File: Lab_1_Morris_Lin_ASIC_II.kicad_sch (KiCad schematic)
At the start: 23 parts, among them J1 Q1_Header, J6 Q1_Header

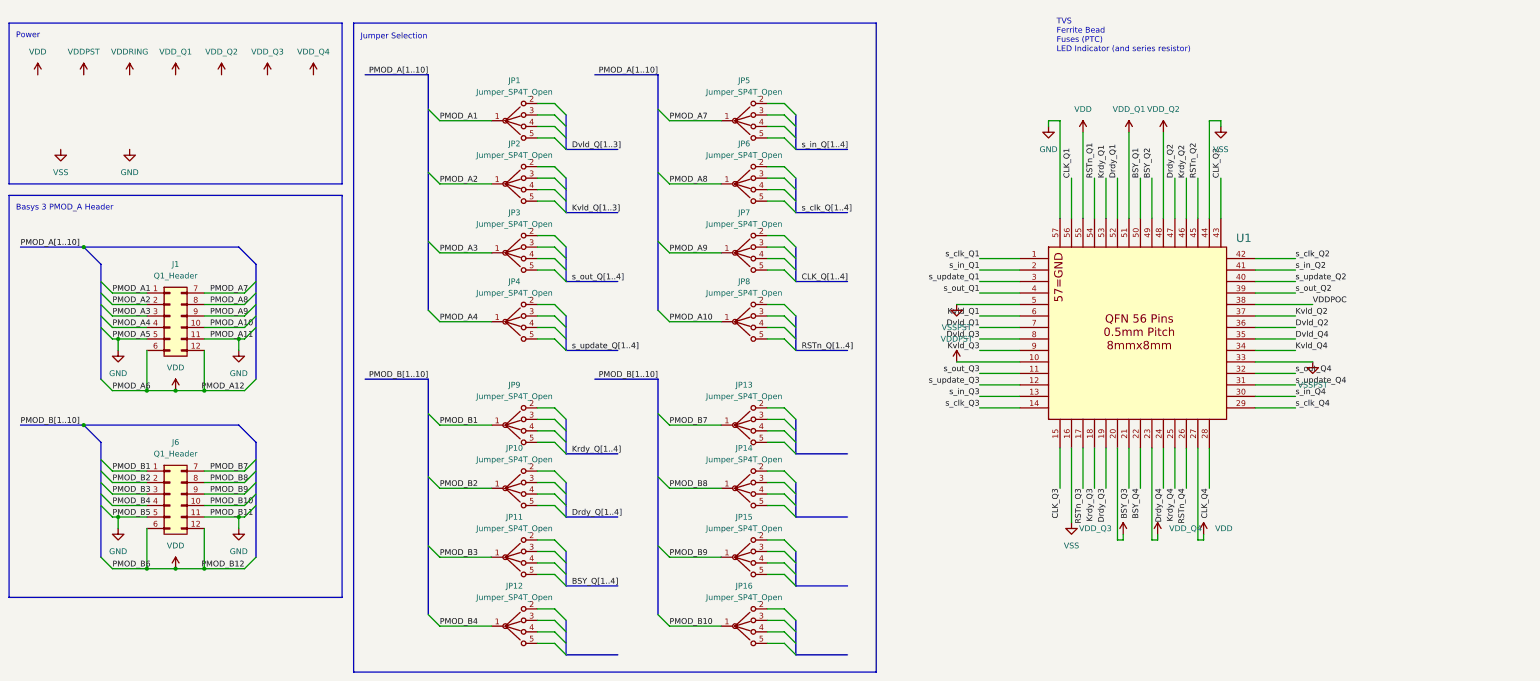
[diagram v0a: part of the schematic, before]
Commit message: Swapped to 1-of-4 Demux IC setup
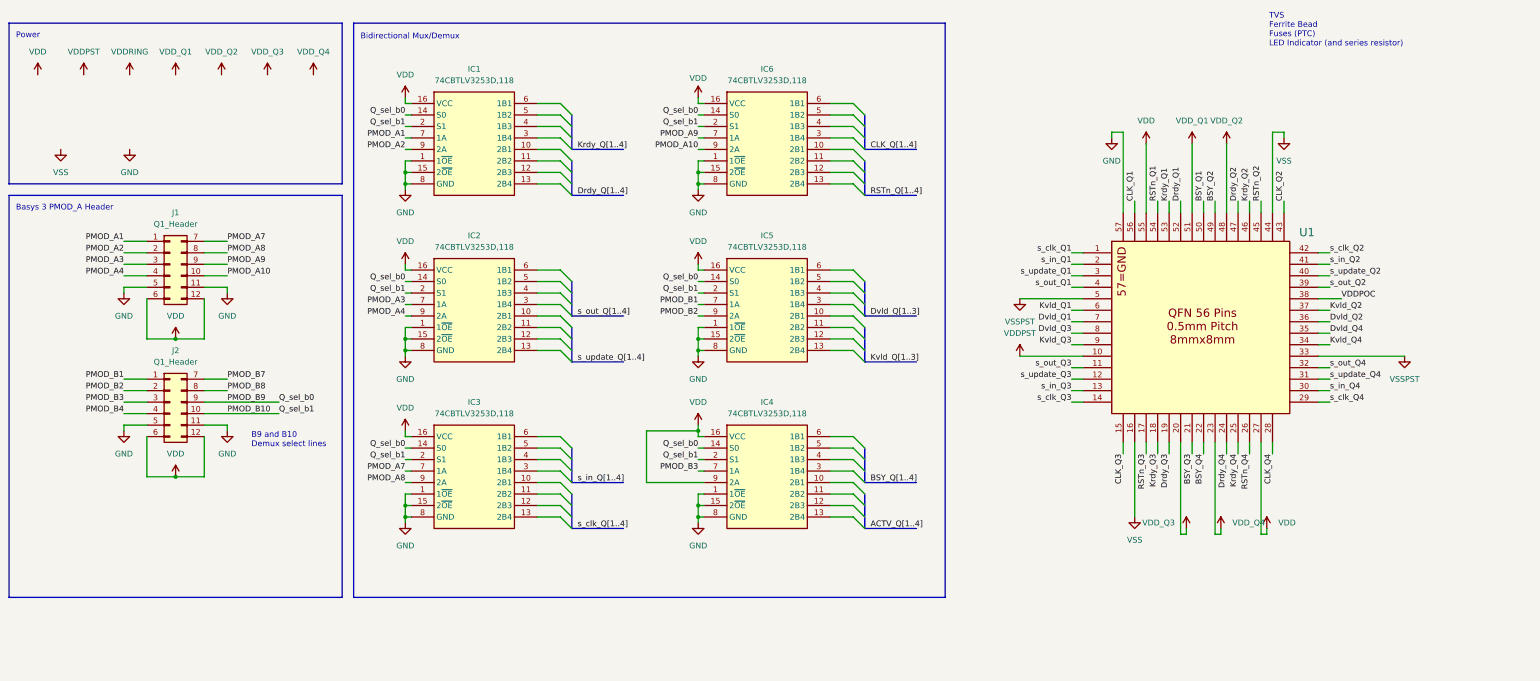
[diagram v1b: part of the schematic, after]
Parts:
- removed J6: Q1_Header, ASIC_II:PinHeader_2x06_P2.54mm_Horizontal, symbol Connector_Generic:Conn_02x06_Top_Bottom
- removed JP1, JP10, JP11, JP12, JP13, JP14, JP15, JP16, JP2, JP3, JP4, JP5, JP6, JP7, JP8, JP9: Jumper_SP4T_Open, ASIC_II:PinHeader_SP4T_1x03_P2.54mm_Vertical, symbol ASIC_II:Jumper_SP4T_Open
- added IC1, IC2, IC3, IC4, IC5, IC6: 74CBTLV3253D,118, SOIC127P600X175-16N, symbol ASIC_II:74CBTLV3253D,118
- added J2: Q1_Header, ASIC_II:PinHeader_2x06_P2.54mm_Horizontal, symbol Connector_Generic:Conn_02x06_Top_Bottom
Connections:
- net GND: now also IC1.1 (1~{OE}), IC1.15 (2~{OE}), IC1.8 (GND), IC2.1 (1~{OE}), IC2.15 (2~{OE}), IC2.8 (GND), IC3.1 (1~{OE}), IC3.15 (2~{OE}), IC3.8 (GND), IC4.1 (1~{OE}), IC4.15 (2~{OE}), IC4.8 (GND), IC5.1 (1~{OE}), IC5.15 (2~{OE}), IC5.8 (GND), IC6.1 (1~{OE}), IC6.15 (2~{OE}), IC6.8 (GND), J2.11 (Pin_11), J2.5 (Pin_5)
- net PMOD_A1: now also IC1.7 (1A)
- net PMOD_A10: now also IC6.9 (2A)
- net PMOD_A2: now also IC1.9 (2A)
- net PMOD_A3: now also IC2.7 (1A)
- net PMOD_A4: now also IC2.9 (2A)
- net PMOD_A7: now also IC3.7 (1A)
- net PMOD_A8: now also IC3.9 (2A)
- net PMOD_A9: now also IC6.7 (1A)
- net PMOD_B1: now also IC5.7 (1A), J2.1 (Pin_1)
- net PMOD_B10: now also IC1.2 (S1), IC2.2 (S1), IC3.2 (S1), IC4.2 (S1), IC5.2 (S1), IC6.2 (S1), J2.10 (Pin_10)
- net PMOD_B2: now also IC5.9 (2A), J2.2 (Pin_2)
- net PMOD_B3: now also IC4.7 (1A), J2.3 (Pin_3)
- net PMOD_B4: now also J2.4 (Pin_4)
- net PMOD_B7: now also J2.7 (Pin_7)
- net PMOD_B8: now also J2.8 (Pin_8)
- net PMOD_B9: now also IC1.14 (S0), IC2.14 (S0), IC3.14 (S0), IC4.14 (S0), IC5.14 (S0), IC6.14 (S0), J2.9 (Pin_9)
- net VDD: now also IC1.16 (VCC), IC2.16 (VCC), IC3.16 (VCC), IC4.16 (VCC), IC4.9 (2A), IC5.16 (VCC), IC6.16 (VCC), J2.12 (Pin_12), J2.6 (Pin_6)
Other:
- note added: "B9 and B10 Demux select lines"
- note added: "Bidirectional Mux/Demux"
- note removed: "Jumper Selection"
- moved on the sheet: J1, U1

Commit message: Started adding LDOs
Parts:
- added JP1, JP2, JP3, JP4: Jumper_3_Open, Connector_PinHeader_2.54mm:PinHeader_1x03_P2.54mm_Vertical, symbol Jumper:Jumper_3_Open
- added U2: TLV75710PDBV, Package_TO_SOT_SMD:SOT-23-5, symbol Regulator_Linear:TLV75710PDBV
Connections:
- net VSS is gone; now on net GND: U1.16, U1.44
- net VSSPST is gone; now on net GND: U1.33, U1.5
- net GND: now also JP1.3 (B), JP2.3 (B), JP3.3 (B), JP4.3 (B), U2.2 (GND)
- net VDD_Q1: now also JP1.2 (C)
- net VDD_Q2: now also JP2.2 (C)
- net VDD_Q3: now also JP3.2 (C)
- net VDD_Q4: now also JP4.2 (C)
- new net LDO_Out: JP1.1 (A), JP2.1 (A), JP3.1 (A), JP4.1 (A), U2.5 (OUT)
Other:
- note added: "B9 and B10 Mux select lines"
- note removed: "B9 and B10 Demux select lines"
- moved on the sheet: J1, J2, U1

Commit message: Starting routing
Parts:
- added C1, C2, C3, C4: 1u, Capacitor_SMD:C_1206_3216Metric_Pad1.33x1.80mm_HandSolder, symbol Device:C
- added C10, C11, C12, C6, C7, C8, C9: 0.1u, Capacitor_SMD:C_1206_3216Metric_Pad1.33x1.80mm_HandSolder, symbol Device:C_Small
- added C5: 10u, Capacitor_SMD:C_1206_3216Metric_Pad1.33x1.80mm_HandSolder, symbol Device:C_Polarized_US
- added D1: Q1, LED_SMD:LED_1206_3216Metric_Pad1.42x1.75mm_HandSolder, symbol Device:LED
- added D2: Q2, LED_SMD:LED_1206_3216Metric_Pad1.42x1.75mm_HandSolder, symbol Device:LED
- added D3: Q3, LED_SMD:LED_1206_3216Metric_Pad1.42x1.75mm_HandSolder, symbol Device:LED
- added D4: Q4, LED_SMD:LED_1206_3216Metric_Pad1.42x1.75mm_HandSolder, symbol Device:LED
- added D5: PTVS3V3S1UR,115, Diode_SMD:Nexperia_CFP3_SOD-123W, symbol ASIC_II:PTVS3V3S1UR,115
- added D6: VDDPOC, LED_SMD:LED_1206_3216Metric_Pad1.42x1.75mm_HandSolder, symbol Device:LED
- added D7: ~{OE}, LED_SMD:LED_1206_3216Metric_Pad1.42x1.75mm_HandSolder, symbol Device:LED
- added D8: VDDPST, LED_SMD:LED_1206_3216Metric_Pad1.42x1.75mm_HandSolder, symbol Device:LED
- added F1: SMDH1206B025TF, Fuse:Fuse_1206_3216Metric_Pad1.42x1.75mm_HandSolder, symbol Device:Polyfuse
- added J1: VDDPST_External, Connector:Banana_Jack_2Pin, symbol Connector_Generic:Conn_01x02
- added J4: VDD_Qn External, Connector:Banana_Jack_1Pin, symbol Connector_Generic:Conn_01x01
- added J5: VDDPST External, Connector:Banana_Jack_1Pin, symbol Connector_Generic:Conn_01x01
- added J6: PMOD_A, ASIC_II:PinHeader_VertNum_2x06_P2.54mm_Vertical, symbol Connector_Generic:Conn_02x06_Top_Bottom
- added J7: PMOD_B, ASIC_II:PinHeader_VertNum_2x06_P2.54mm_Vertical, symbol Connector_Generic:Conn_02x06_Top_Bottom
- added JP1, JP2, JP3, JP5, JP6, JP9: Jumper_3_Open, Connector_PinHeader_2.54mm:PinHeader_1x03_P2.54mm_Vertical, symbol Jumper:Jumper_3_Open
- added Q1: BSS138, Package_TO_SOT_SMD:SOT-23, symbol Transistor_FET:BSS138
- added R1, R2, R3, R4, R7, R8, R9: 470, Resistor_SMD:R_1206_3216Metric_Pad1.30x1.75mm_HandSolder, symbol Device:R_US
- added R10, R11, R12, R13, R14, R15, R16, R17, R18, R19, R20, R21, R22, R23, R24, R25, R26, R27, R28, R29, R30, R31, R32, R33, R34, R35, R36, R37, R38, R5, R6: 10k, Resistor_SMD:R_1206_3216Metric_Pad1.30x1.75mm_HandSolder, symbol Device:R_US
- added TP1, TP2, TP3, TP4, TP5, TP6: TestPoint, TestPoint:TestPoint_Loop_D2.54mm_Drill1.5mm_Beaded, symbol Connector:TestPoint
- added U1: TLV75710PDBV, Package_TO_SOT_SMD:SOT-23-5, symbol Regulator_Linear:TLV75710PDBV
- IC1, IC2, IC3, IC5: footprint SOIC127P600X175-16N -> ASIC_II:SOIC127P600X175-16N
- IC4: renamed from IC6; footprint SOIC127P600X175-16N -> ASIC_II:SOIC127P600X175-16N
- IC6: renamed from IC4; footprint SOIC127P600X175-16N -> ASIC_II:SOIC127P600X175-16N
- J2: renamed from J1; value Q1_Header -> PMOD_A; now left out of the parts list
- J3: renamed from J2; value Q1_Header -> PMOD_B; now left out of the parts list
- renumbered JP4 to JP10, JP1 to JP4, JP2 to JP7, JP3 to JP8, U1 to U3
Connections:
- net BSY_Q1: now also IC6.6 (1B1)
- net BSY_Q2: now also IC6.5 (1B2)
- net BSY_Q3: now also IC6.4 (1B3)
- net BSY_Q4: now also IC6.3 (1B4)
- net CLK_Q1: now also IC4.6 (1B1), R31.1
- net CLK_Q2: now also IC4.5 (1B2), R33.1
- net CLK_Q3: now also IC4.4 (1B3), R35.1
- net CLK_Q4: now also IC4.3 (1B4), R37.1
- net Drdy_Q1: now also IC1.10 (2B1), R12.1
- net Drdy_Q2: now also IC1.11 (2B2), R17.1
- net Drdy_Q3: now also IC1.12 (2B3), R22.1
- net Drdy_Q4: now also IC1.13 (2B4), R27.1
- net Dvld_Q1: now also IC5.6 (1B1)
- net Dvld_Q2: now also IC5.5 (1B2)
- net Dvld_Q3: now also IC5.4 (1B3)
- net Dvld_Q4: now also IC5.3 (1B4)
- net GND: now also C1.2, C10.1, C11.2, C12.1, C2.2, C3.2, C4.2, C5.2, C6.2, C7.1, C8.1, C9.1, D1.1 (K), D2.1 (K), D3.1 (K), D4.1 (K), D5.2 (A), D7.1 (K), D8.1 (K), J1.2 (Pin_2), J6.12 (Pin_12), J6.6 (Pin_6), J7.12 (Pin_12), J7.6 (Pin_6), JP5.3 (B), JP6.3 (B), JP9.3 (B), Q1.2 (S), R10.2, R11.2, R12.2, R13.2, R14.2, R15.2, R16.2, R17.2, R18.2, R19.2, R20.2, R21.2, R22.2, R23.2, R24.2, R25.2, R26.2, R27.2, R28.2, R29.2, R30.2, R31.2, R33.2, R35.2, R37.2, R5.2, TP4.1, TP5.1, TP6.1, U1.2 (GND); no longer IC1.1 (1~{OE}), IC1.15 (2~{OE}), IC2.1 (1~{OE}), IC2.15 (2~{OE}), IC3.1 (1~{OE}), IC3.15 (2~{OE}), IC4.1 (1~{OE}), IC4.15 (2~{OE}), IC5.1 (1~{OE}), IC5.15 (2~{OE}), IC6.1 (1~{OE}), IC6.15 (2~{OE})
- net Krdy_Q1: now also IC1.6 (1B1), R11.1
- net Krdy_Q2: now also IC1.5 (1B2), R16.1
- net Krdy_Q3: now also IC1.4 (1B3), R21.1
- net Krdy_Q4: now also IC1.3 (1B4), R26.1
- net Kvld_Q1: now also IC5.10 (2B1)
- net Kvld_Q2: now also IC5.11 (2B2)
- net Kvld_Q3: now also IC5.12 (2B3)
- net Kvld_Q4: now also IC5.13 (2B4)
- net PMOD_A1: now also J6.1 (Pin_1)
- net PMOD_A10: now also J6.10 (Pin_10); no longer IC4.9 (2A)
- net PMOD_A2: now also J6.2 (Pin_2)
- net PMOD_A3: now also J6.3 (Pin_3)
- net PMOD_A4: now also J6.4 (Pin_4)
- net PMOD_A7: now also J6.7 (Pin_7)
- net PMOD_A8: now also J6.8 (Pin_8)
- net PMOD_A9: now also J6.9 (Pin_9); no longer IC4.7 (1A)
- net PMOD_B1: now also IC4.7 (1A), J7.1 (Pin_1); no longer IC5.7 (1A)
- net PMOD_B10: now also J7.10 (Pin_10); no longer IC1.2 (S1), IC2.2 (S1), IC3.2 (S1), IC4.2 (S1), IC5.2 (S1), IC6.2 (S1)
- net PMOD_B2: now also IC4.9 (2A), J7.2 (Pin_2); no longer IC5.9 (2A)
- net PMOD_B3: now also IC5.7 (1A), J7.3 (Pin_3); no longer IC6.7 (1A)
- net PMOD_B4: now also IC5.9 (2A), J7.4 (Pin_4)
- net PMOD_B7: now also IC6.7 (1A), J7.7 (Pin_7)
- net PMOD_B8: now also J7.8 (Pin_8)
- net PMOD_B9: now also J7.9 (Pin_9); no longer IC1.14 (S0), IC2.14 (S0), IC3.14 (S0), IC4.14 (S0), IC5.14 (S0), IC6.14 (S0)
- net RSTn_Q1: now also IC4.10 (2B1), R32.2
- net RSTn_Q2: now also IC4.11 (2B2), R34.2
- net RSTn_Q3: now also IC4.12 (2B3), R36.2
- net RSTn_Q4: now also IC4.13 (2B4), R38.2
- net VDD: now also C12.2, C7.2, JP3.2 (C), TP1.1; no longer IC1.16 (VCC), IC2.16 (VCC), IC3.16 (VCC), IC4.16 (VCC), IC5.16 (VCC), IC6.16 (VCC), IC6.9 (2A), J2.12 (Pin_12), J2.6 (Pin_6), J3.12 (Pin_12), J3.6 (Pin_6)
- net VDDPOC: now also Q1.1 (G)
- net VDDPST: now also IC1.16 (VCC), IC2.16 (VCC), IC3.16 (VCC), IC4.16 (VCC), IC5.16 (VCC), IC6.16 (VCC), IC6.9 (2A), U2.1 (IN), U2.3 (EN), C1.1, C2.1, C5.1, C6.1, D5.1 (K), F1.1, JP5.1 (A), JP6.1 (A), JP9.1 (A), R32.1, R34.1, R36.1, R38.1, R6.1, R7.1, R8.1, R9.1, TP2.1, U1.1 (IN), U1.3 (EN)
- net VDD_Q1: now also C9.2
- net VDD_Q2: now also C11.1
- net VDD_Q3: now also C8.2
- net VDD_Q4: now also C10.2
- net s_clk_Q1: now also IC3.10 (2B1), R15.1
- net s_clk_Q2: now also IC3.11 (2B2), R20.1
- net s_clk_Q3: now also IC3.12 (2B3), R25.1
- net s_clk_Q4: now also IC3.13 (2B4), R30.1
- net s_in_Q1: now also IC3.6 (1B1), R14.1
- net s_in_Q2: now also IC3.5 (1B2), R19.1
- net s_in_Q3: now also IC3.4 (1B3), R24.1
- net s_in_Q4: now also IC3.3 (1B4), R29.1
- net s_out_Q1: now also IC2.10 (2B1)
- net s_out_Q2: now also IC2.11 (2B2)
- net s_out_Q3: now also IC2.12 (2B3)
- net s_out_Q4: now also IC2.13 (2B4)
- net s_update_Q1: now also IC2.6 (1B1), R13.1
- net s_update_Q2: now also IC2.5 (1B2), R18.1
- net s_update_Q3: now also IC2.4 (1B3), R23.1
- net s_update_Q4: now also IC2.3 (1B4), R28.1
- net LED_Q1: now reaches IC6.10 (2B1)
- net LED_Q1: now also R1.1
- net LED_Q2: now reaches IC6.11 (2B2)
- net LED_Q2: now also R2.1
- net LED_Q3: now reaches IC6.12 (2B3)
- net LED_Q3: now also R3.1
- net LED_Q4: now reaches IC6.13 (2B4)
- net LED_Q4: now also R4.1
- net LDO_Out: no longer names the net of JP10.1 (A), JP4.1 (A), JP7.1 (A), JP8.1 (A)
- net LDO_Out: now also JP2.2 (C), TP3.1; no longer U2.5 (OUT)
- new net: C3.1, JP3.3 (B), U1.5 (OUT)
- new net: D2.2 (A), R2.2
- new net: J1.1 (Pin_1), JP1.3 (B)
- new net: D1.2 (A), R1.2
- new net: J5.1 (Pin_1), JP3.1 (A)
- new net: D4.2 (A), R4.2
- new net: J4.1 (Pin_1), JP2.1 (A)
- new net: D7.2 (A), R8.2
- new net: F1.2, JP1.2 (C)
- new net: D6.2 (A), R7.2
- new net: C4.1, JP2.3 (B), U2.5 (OUT)
- new net: D6.1 (K), Q1.3 (D)
- new net: D3.2 (A), R3.2
- new net: D8.2 (A), R9.2
- new net SEL_b0: IC1.14 (S0), IC2.14 (S0), IC3.14 (S0), IC4.14 (S0), IC5.14 (S0), IC6.14 (S0), JP5.2 (C), R5.1
- new net SEL_b1: IC1.2 (S1), IC2.2 (S1), IC3.2 (S1), IC4.2 (S1), IC5.2 (S1), IC6.2 (S1), JP9.2 (C), R10.1
- new net VDDPMOD: J2.12 (Pin_12), J2.6 (Pin_6), J3.12 (Pin_12), J3.6 (Pin_6), JP1.1 (A)
- new net ~{OE}: IC1.1 (1~{OE}), IC1.15 (2~{OE}), IC2.1 (1~{OE}), IC2.15 (2~{OE}), IC3.1 (1~{OE}), IC3.15 (2~{OE}), IC4.1 (1~{OE}), IC4.15 (2~{OE}), IC5.1 (1~{OE}), IC5.15 (2~{OE}), IC6.1 (1~{OE}), IC6.15 (2~{OE}), JP6.2 (C), R6.2
- no-connect marks 0 -> 4
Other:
- note added: "ASIC I/II AES-128 Encode/Decode Chip"
- note added: "Basys 3 PMOD Headers"
- note added: "Debug Headers"
- note added: "Output Disabled LED"
- note added: "Pull-Down / Pull-Up Pins"
- note added: "Select Lines and ~{OE}"
- note added: "Select Lines and ~{OE} Indicator LEDs"
- note added: "VDDPOC Indicator LED Buffered"
- note added: "VDDPST Indicator LED"
- note added: "VDDPST Source & Protections"
- note added: "VDDRING from PMOD or External"
- note added: "VDD_Qn from LDO/External and Quadrant Selection"
- note removed: "B9 and B10 Mux select lines"
- note removed: "Basys 3 PMOD_A Header"
- note removed: "Power"
- note removed: "TVS Ferrite Bead Fuses (PTC) LED Indicator (and series resistor)"
- moved on the sheet: H1, H2, H3, H4, IC1, IC2, IC3, IC4, IC5, IC6, J2, J3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
